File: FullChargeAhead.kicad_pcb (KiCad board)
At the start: 2 copper layers, 18 parts, among them P101 USB_OTG, P102 CONN_01X02, P103 CONN_01X02, U101 MCP73834-FCI/UN

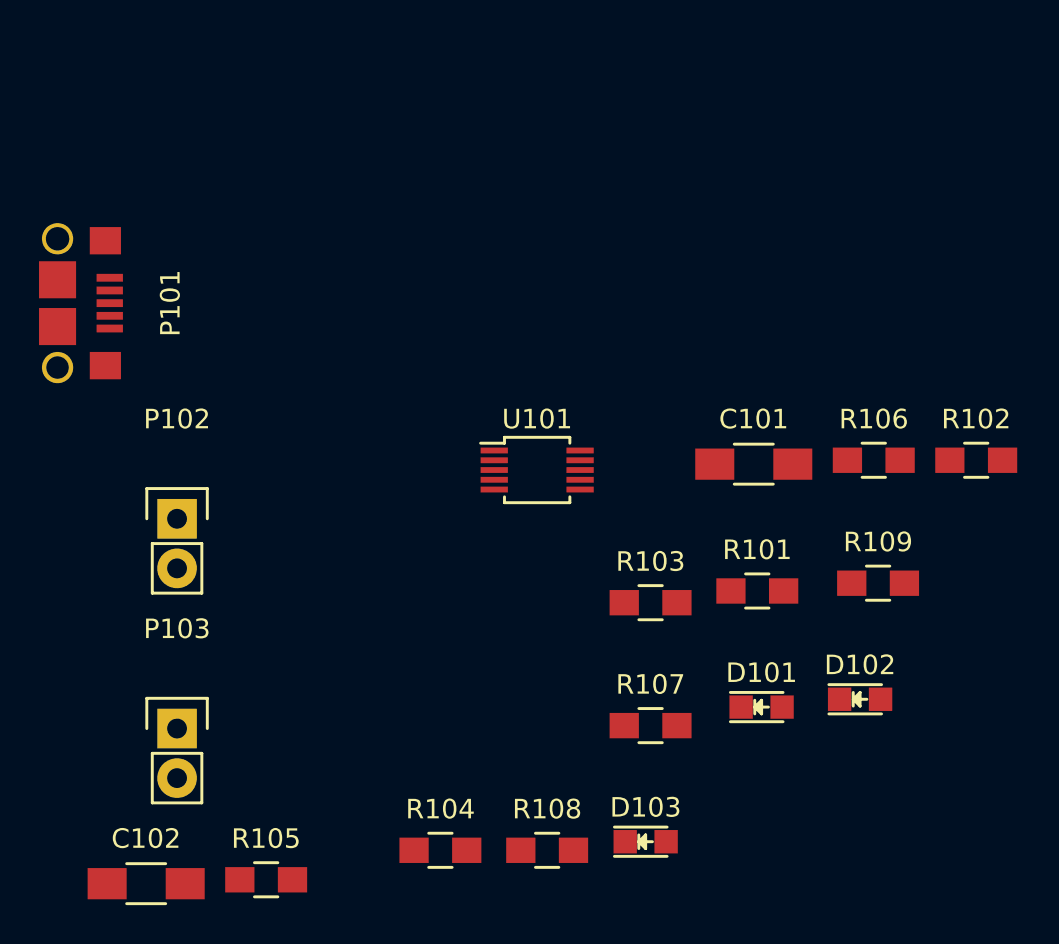
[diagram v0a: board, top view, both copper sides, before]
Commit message: PBC finished and submitted to OSH park. Note the board is smaller than CE example and may not work as well as a result.
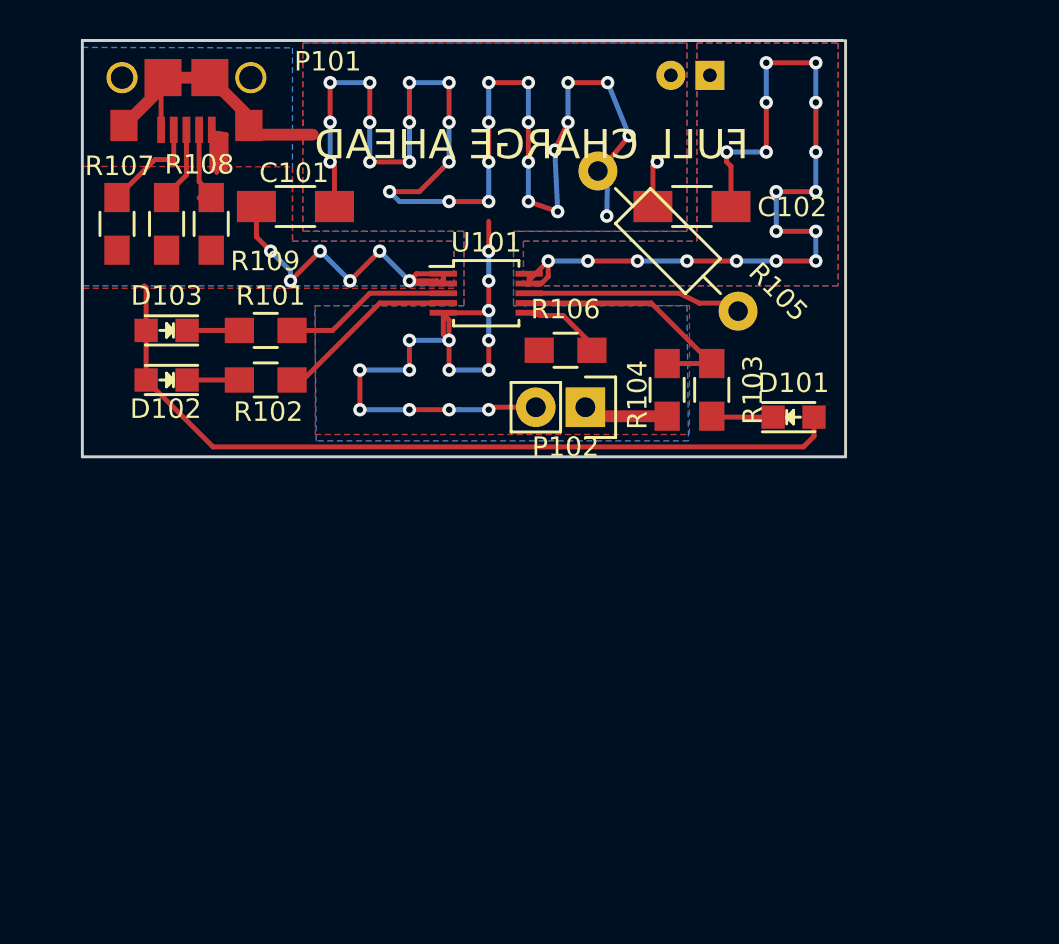
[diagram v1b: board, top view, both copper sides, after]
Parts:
- P103: footprint Pin_Headers:Pin_Header_Straight_1x02 -> Footprints:JST_2Pin; moved to B.Cu
- R105: footprint Resistors_SMD:R_0805_HandSoldering -> Resistors_ThroughHole:Resistor_Horizontal_RM10mm
- moved C102 44.6 mm to (167.9, 87.6), turned to 180 degrees
- moved P103 43.2 mm to (168.8, 80.9), turned to 90 degrees
- moved R105 40.1 mm to (163.1, 85.8), turned to 315 degrees
- moved D102 39.1 mm to (141.0, 96.5), turned to 180 degrees
- moved R109 38.8 mm to (143.3, 88.5), turned to 90 degrees
- moved R108 37.6 mm to (141.0, 88.5), turned to 90 degrees
- moved R107 37.5 mm to (138.4, 88.5), turned to 90 degrees
- moved R102 36.6 mm to (146.1, 96.5), turned to 180 degrees
- moved D103 35.9 mm to (141.0, 94.0), turned to 180 degrees
- moved R101 28.5 mm to (146.1, 94.0), turned to 180 degrees
- moved C101 26.9 mm to (147.6, 87.6)
- moved R104 26.3 mm to (166.6, 97.0), turned to 270 degrees
- moved P102 21.7 mm to (162.4, 97.9), turned to 270 degrees
- moved R106 16.8 mm to (161.4, 95.0)
- moved D101 14.9 mm to (173.1, 98.4)
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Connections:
- net Net-(C102-Pad1) renamed /Vbat
- C101 pad 1: Net-(C101-Pad1) -> /Vdd
- D101 pad 2: Net-(C101-Pad1) -> /Vdd
- D102 pad 2: Net-(C101-Pad1) -> /Vdd
- D103 pad 2: Net-(C101-Pad1) -> /Vdd
- P101 pad 1: Net-(C101-Pad1) -> /Vdd
- R107 pad 1: GND -> /Vdd
- R108 pad 1: GND -> /Vdd
- R109 pad 1: GND -> /Vdd
- U101 pad 1: Net-(C101-Pad1) -> /Vdd
- U101 pad 2: Net-(C101-Pad1) -> /Vdd
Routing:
- net GND: track 0.00 -> 116.8 mm, vias 0 -> 44
- net /Vdd: track 0.00 -> 73.5 mm, vias 0 -> 6
- net /Vbat: track 0.00 -> 43.9 mm, vias 0 -> 18
- net Net-(R103-Pad1): track 0.00 -> 12.9 mm
- net Net-(R105-Pad2): track 0.00 -> 10.0 mm
- net Net-(R102-Pad1): track 0.00 -> 9.39 mm
- net Net-(R101-Pad1): track 0.00 -> 8.54 mm
- net Net-(P101-Pad4): track 0.00 -> 5.48 mm
- net Net-(P101-Pad2): track 0.00 -> 4.60 mm
- net Net-(P102-Pad1): track 0.00 -> 4.38 mm
- net Net-(R106-Pad2): track 0.00 -> 4.14 mm
- net Net-(P101-Pad3): track 0.00 -> 3.89 mm
- net Net-(D101-Pad1): track 0.00 -> 3.16 mm
- net Net-(D103-Pad1): track 0.00 -> 2.68 mm
- net Net-(D102-Pad1): track 0.00 -> 2.68 mm
- added copper zone on B.Cu, net /Vbat
- added copper zone on F.Cu, net /Vbat
- added copper zone on B.Cu, net /Vdd
- added copper zone on F.Cu, net /Vdd
- added copper zone on B.Cu, net GND
- added copper zone on F.Cu, net GND
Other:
- board outline added: 39.1 x 21.3 mm
- net class Default: clearance 0.2 -> 0.1524; trace_width 0.25 -> 0.1524; via_dia 0.6 -> 0.6858; via_drill 0.4 -> 0.3302
- rule trace_clearance: 0.2 -> 0.1524
- rule trace_min: 0.2 -> 0.1524
- rule via_min_drill: 0.3 -> 0.3302
- rule via_min_size: 0.4 -> 0.6858
- board text added: "FULL CHARGE AHEAD"
